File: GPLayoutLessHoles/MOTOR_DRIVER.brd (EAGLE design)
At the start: 170 x 45.4 mm, 95 parts, among them T1 2N2222, T2 2N2222, U7 ATMEGA328P_TQFP, Y1 16MHz

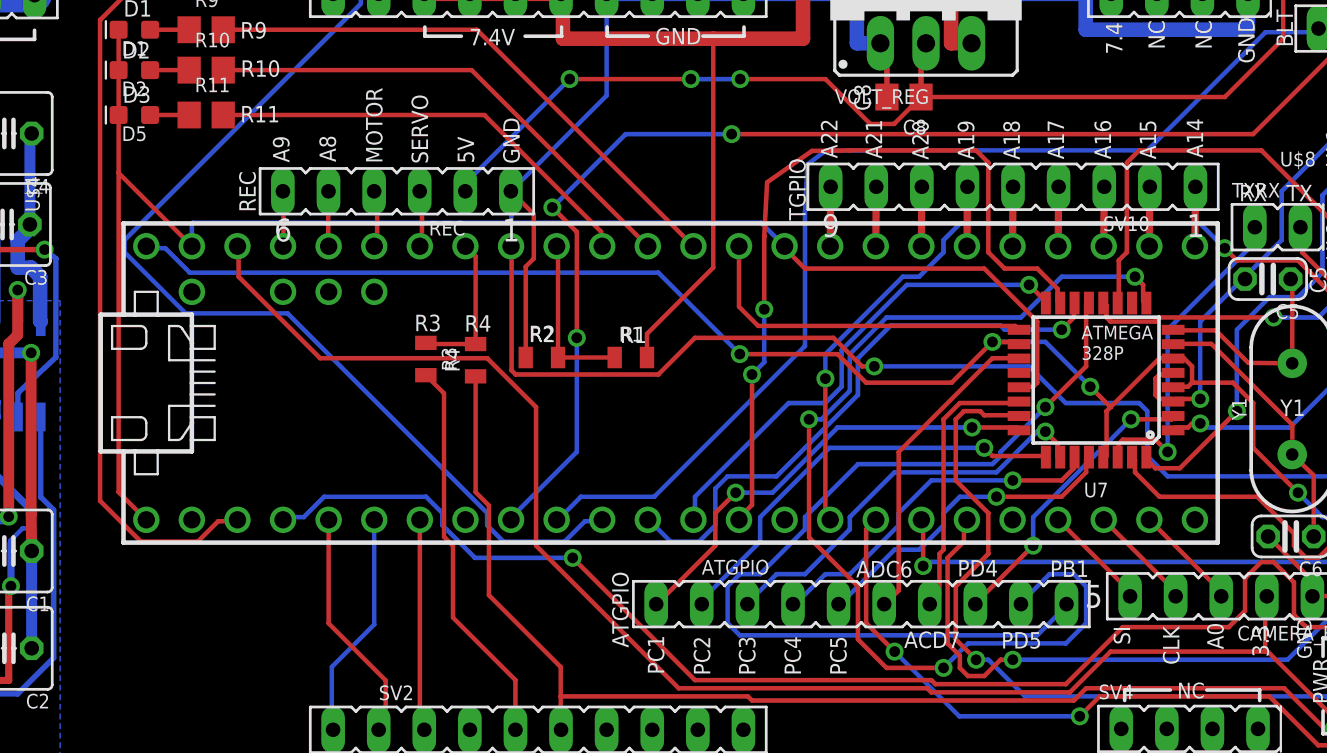
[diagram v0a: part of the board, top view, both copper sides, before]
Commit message: reduced GPIOs on teensy and started on atmega
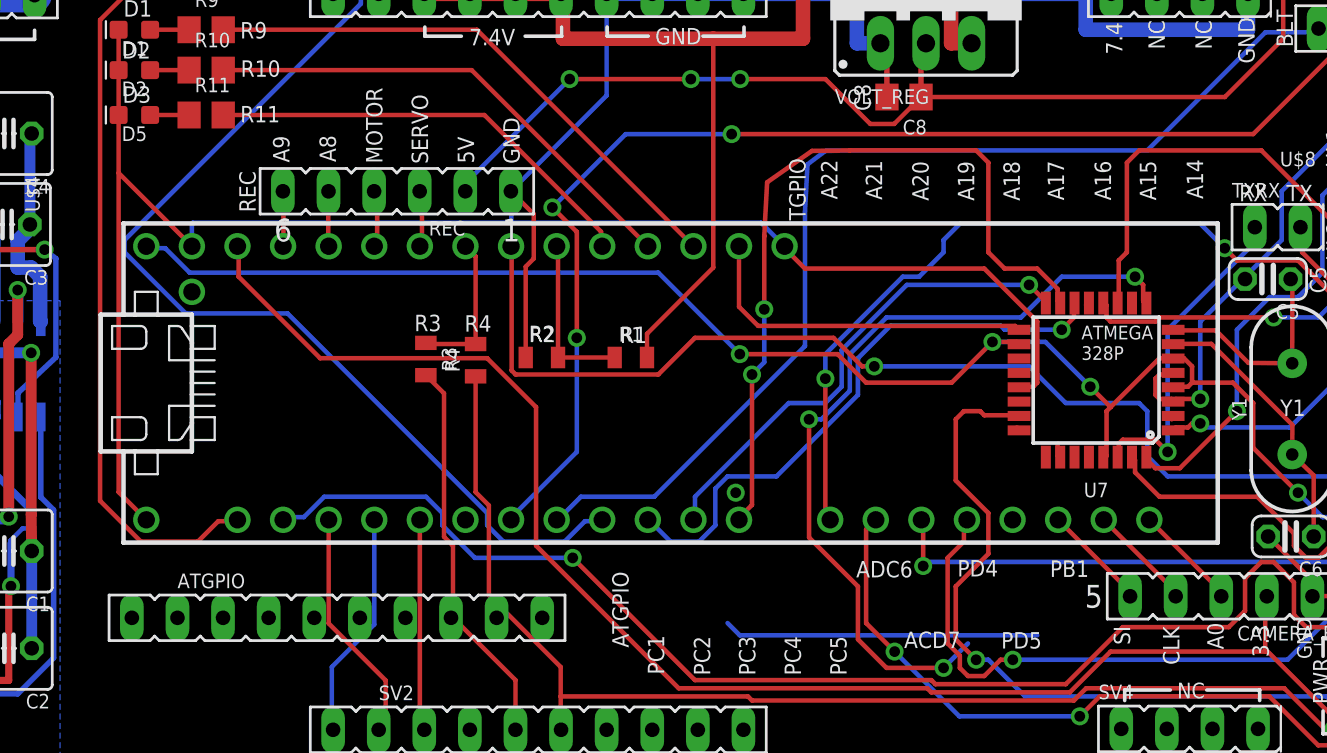
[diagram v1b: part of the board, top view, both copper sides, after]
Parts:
- removed SV10: (no value), con-lsta:FE09
- U$1: value TEENSY_3.5/3.6_BASIC -> TEENSY_3.5/3.6_FEWER; device Teensy356:TEENSY_3.5/3.6_BASIC -> Teensy356:TEENSY_3.5/3.6_BASIC_FEWER_PIN
- moved ATGPIO 29.2 mm to (54.3, 8.24)
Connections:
- removed net TGPIO1: SV10.1, U$1.33/A14
- removed net TGPIO2: SV10.2, U$1.34/A15
- removed net TGPIO3: SV10.3, U$1.35/A16
- removed net TGPIO4: SV10.4, U$1.36/A17
- removed net TGPIO5: SV10.5, U$1.37/A18
- removed net TGPIO6: SV10.6, U$1.38/A19
- removed net TGPIO7: SV10.7, U$1.39/A20
- removed net TGPIO8: SV10.8, U$1.21/DAC0
- removed net TGPIO9: SV10.9, U$1.A22/DAC1
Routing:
- net PB1: track 51.2 -> 17.7 mm, vias 1 -> 0
- net PC1: track 25.4 -> 0.20 mm, vias 2 -> 1
- net PC2: track 24.1 -> 0.07 mm, vias 1 -> 0
- net PC3: track 22.8 -> 0.84 mm, vias 1 -> 0
- net PC4: track 19.8 -> 0.17 mm, vias 1 -> 0
- net PC5: track 18.1 -> 0.00 mm, vias 1 -> 0
- net ADC6: track 17.7 -> 0.12 mm
- net PD4: track 16.4 -> 0.20 mm, vias 2 -> 0
- net ADC7: track 15.2 -> 0.14 mm
- net PD5: track 58.9 -> 45.1 mm
- net TGPIO9: track 3.31 -> 0.00 mm
- net TGPIO8: track 3.31 -> 0.00 mm
- net TGPIO7: track 3.31 -> 0.00 mm
- net TGPIO6: track 3.31 -> 0.00 mm
- net TGPIO5: track 3.31 -> 0.00 mm
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
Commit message: more edits
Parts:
- SV2: device con-lsta:FE10 -> con-lsta:FE05-1
- moved ATGPIO 33.7 mm to (86.0, -2.94)
- moved SV2 6.33 mm to (59.2, 1.97)
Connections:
- net MOTOR_HIGH: now also SV2.4; no longer SV2.5
- net MOTOR_LOW: now also SV2.5; no longer SV2.6
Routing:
- net MOTOR_LOW: track 104.3 -> 106.8 mm
- net MOTOR_HIGH: track 21.8 -> 20.9 mm

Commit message: more edits
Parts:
- 3_3V, 5V: device con-lsta:FE05-1 -> con-lstb:MA03-1
- GROUND: device con-lsta:FE05-1 -> con-lsta:FE04-1
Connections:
- net 3_3V: no longer 3_3V.4, 3_3V.5
- net 5V: no longer 5V.4, 5V.5
- net GND: no longer GROUND.5
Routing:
- net 5V: track 124.3 -> 115.8 mm
- net GND: track 284.7 -> 279.5 mm

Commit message: more edits
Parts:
- C5, C6: device resistor:C025-024X044 -> rcl:C0603
- CAMERA_B: device con-lsta:FE05-1 -> con-lstb:MA03-1
- moved ATGPIO 12.2 mm to (83.5, 8.95)
- moved CAMERA_B 2.75 mm to (100.8, 9.29)
- moved C6 0.15 mm to (107.6, 12.8)
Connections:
- net 3_3V: no longer CAMERA_B.2
- net CAMERA_A0_B: now also CAMERA_B.1; no longer CAMERA_B.3
- net CAMERA_CL_B: now also CAMERA_B.2; no longer CAMERA_B.4
- net CAMERA_SI_B: now also CAMERA_B.3; no longer CAMERA_B.5
- net GND: no longer CAMERA_B.1
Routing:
- net GND: track 279.5 -> 287.7 mm, vias 1 -> 2
- net HALL2_B: track 101.0 -> 95.9 mm
- net 3_3V: track 156.9 -> 152.6 mm
- net TX: track 33.9 -> 34.6 mm

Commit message: more edits. will try rerouting top after this one
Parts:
- moved 3_3V 2.29 mm to (119.8, 3.00)
- moved 5V 1.08 mm to (118.6, 5.85)
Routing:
- net 3_3V: track 152.6 -> 70.2 mm
- net PC1: track 0.20 -> 27.6 mm, vias 1 -> 2
- net PB1: track 17.7 -> 44.5 mm, vias 0 -> 1
- net PC2: track 0.07 -> 22.8 mm, vias 0 -> 1
- net PC3: track 0.84 -> 23.5 mm, vias 0 -> 1
- net PC4: track 0.17 -> 20.5 mm, vias 0 -> 1
- net ADC6: track 0.12 -> 19.8 mm
- net PC5: track 0.00 -> 19.6 mm, vias 0 -> 1
- net PD4: track 0.20 -> 16.5 mm, vias 0 -> 2
- net ADC7: track 0.14 -> 16.1 mm
- net PD5: track 45.1 -> 59.3 mm
- net 5V: track 115.8 -> 124.0 mm
- net LED2HI: track 13.3 -> 14.0 mm
- net CAMERA_CL_B: track 5.67 -> 6.34 mm
- net CAMERA_SI_B: track 5.67 -> 6.34 mm
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
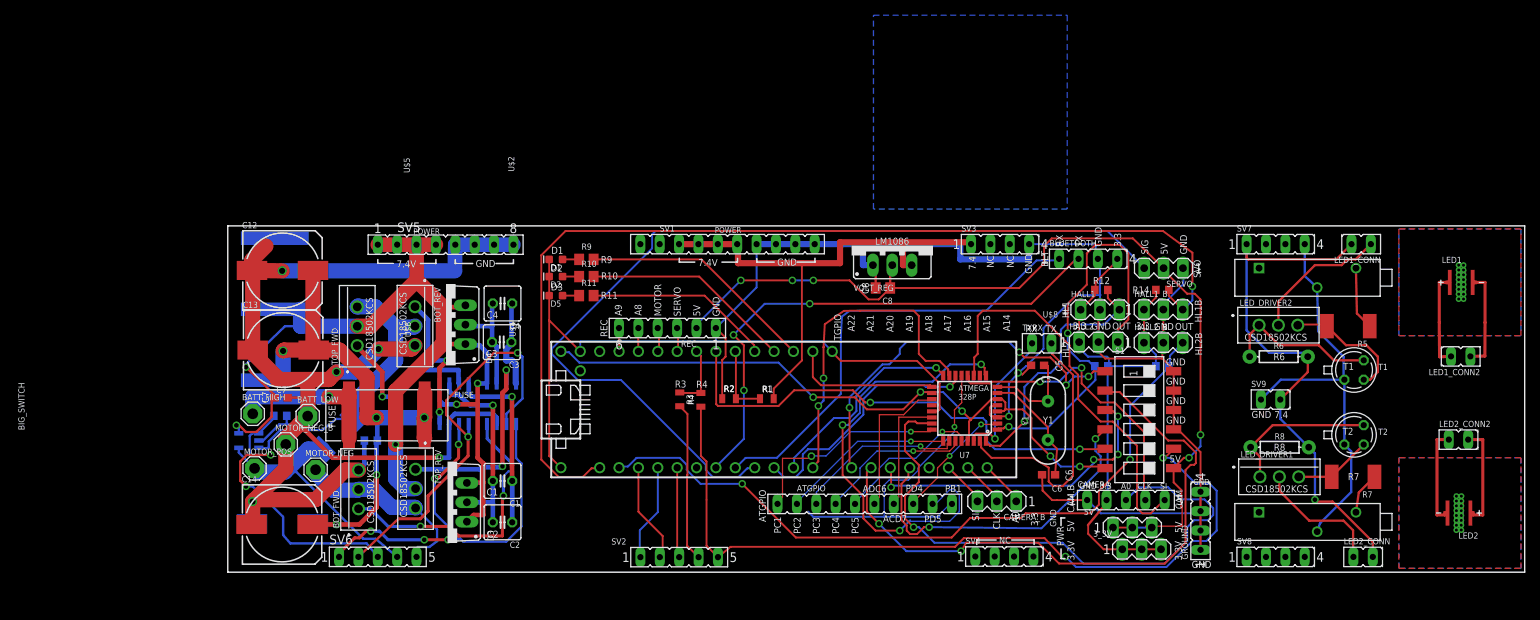
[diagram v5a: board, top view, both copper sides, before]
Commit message: new caps rerouted a lot, thinner wires, wider clearances
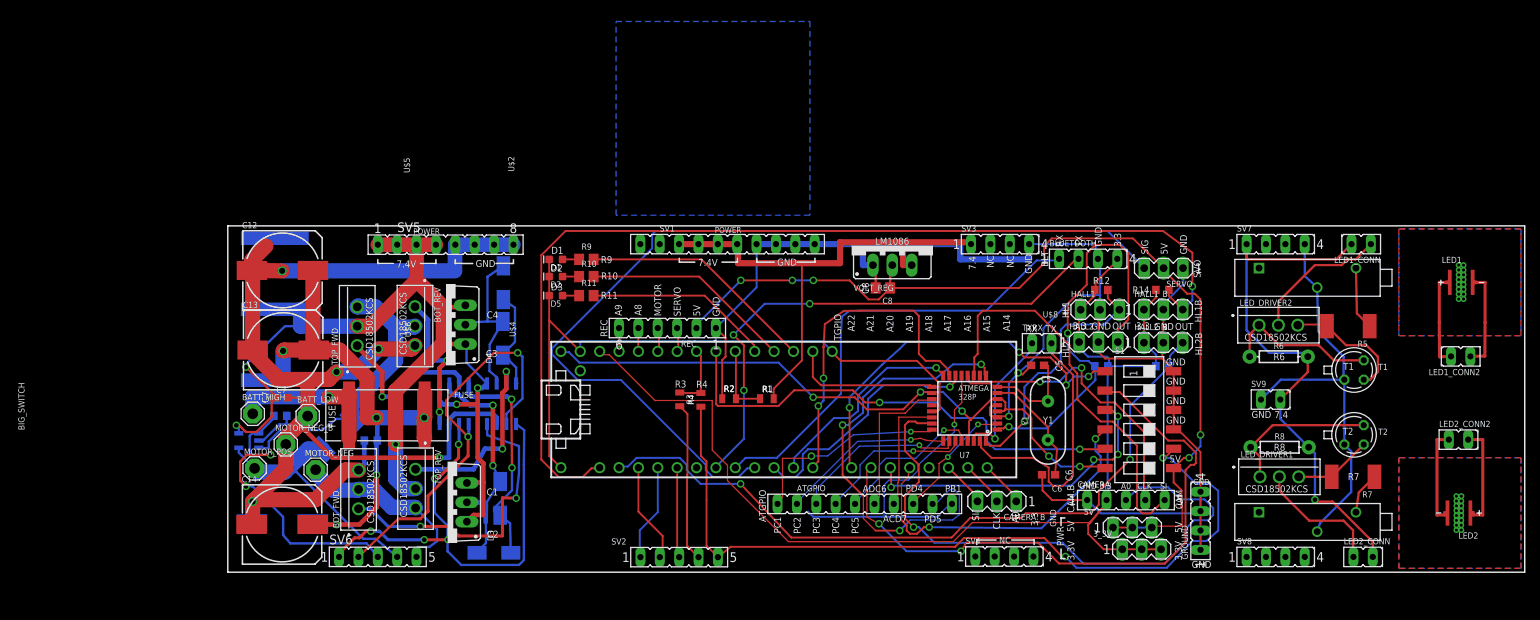
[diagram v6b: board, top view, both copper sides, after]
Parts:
- C1, C2, C3, C4: device resistor:C025-050X050 -> cap-aluminum:CAP_EEE_B
- moved C2 4.15 mm to (34.9, 2.55), flipped to the bottom, turned to 0 degrees
- moved C4 2.72 mm to (36.1, 37.9), flipped to the bottom, turned to 90 degrees
- moved C1 2.31 mm to (35.7, 9.67), flipped to the bottom, turned to 90 degrees
- moved C3 0.52 mm to (36.0, 30.7), flipped to the bottom, turned to 90 degrees
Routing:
- net 3_3V: track 70.2 -> 150.9 mm
- net N$12: track 14.4 -> 22.5 mm
- net LI_TOP: track 58.9 -> 64.9 mm
- net N$4: track 23.6 -> 29.3 mm, vias 1 -> 2
- net N$5: track 26.3 -> 30.6 mm, vias 1 -> 2
- net N$9: track 37.1 -> 39.9 mm
- net N$11: track 11.8 -> 14.4 mm
- net 7_4V_TOP: track 138.1 -> 136.8 mm
- net N$10: track 26.2 -> 25.3 mm
- net N$3: track 21.3 -> 20.5 mm
- net PC5: track 19.6 -> 20.2 mm
